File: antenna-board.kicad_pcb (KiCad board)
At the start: 2 copper layers, 42.4 x 42.4 mm, 2 parts, among them J1 Conn_01x01, U1 U.FLport

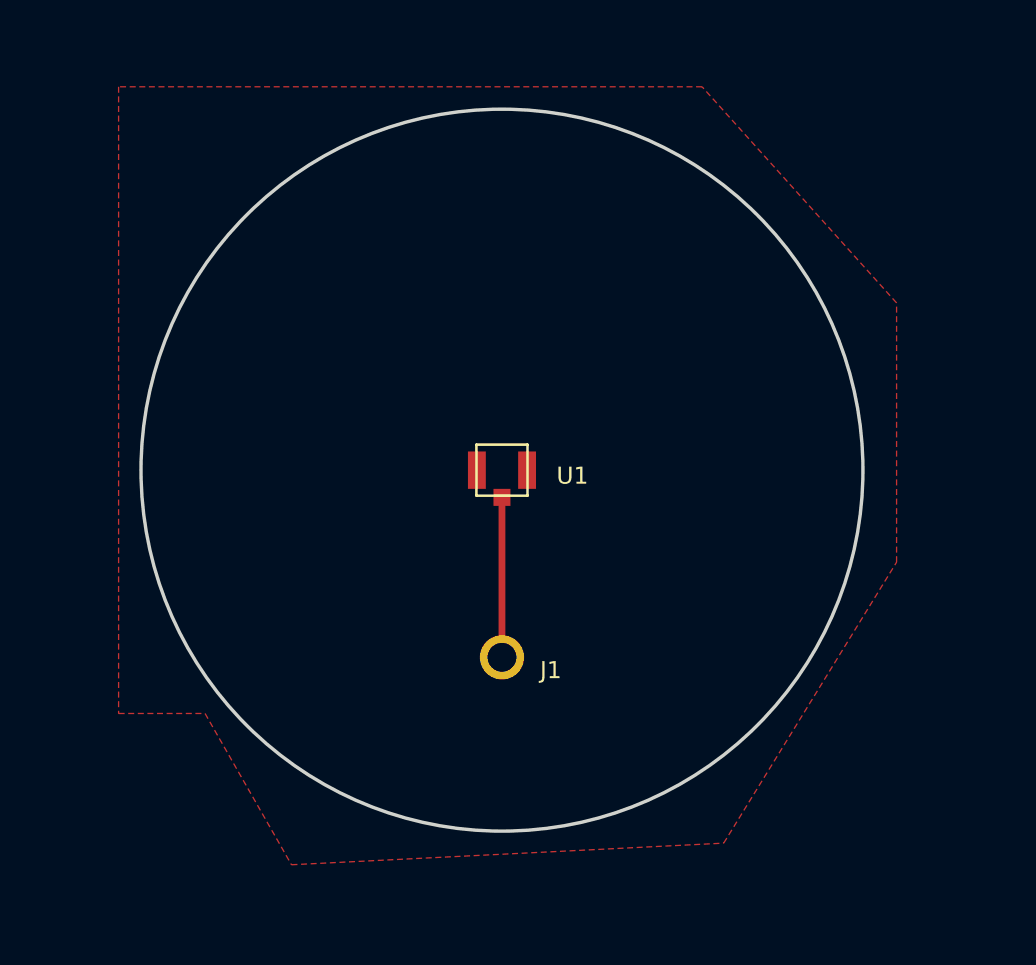
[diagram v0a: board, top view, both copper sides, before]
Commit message: Updated Trace Width and GNDs
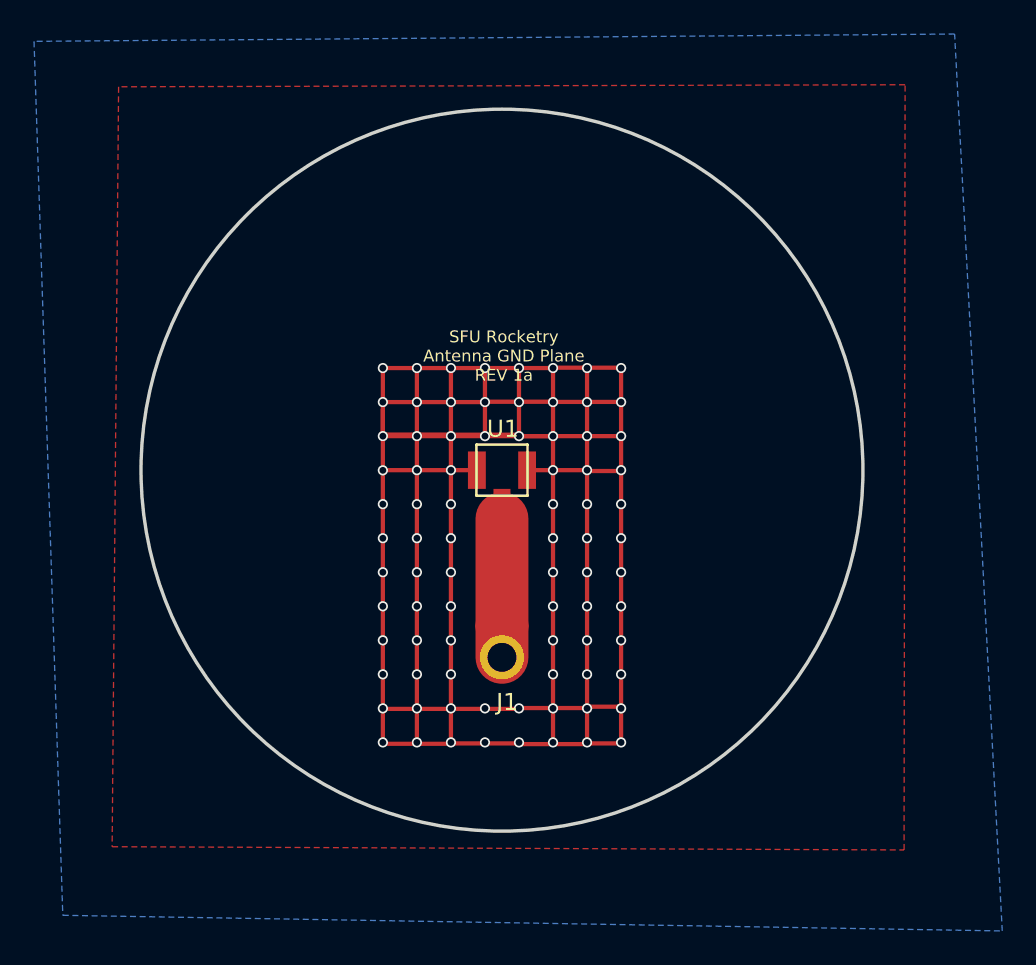
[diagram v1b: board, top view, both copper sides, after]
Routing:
- net GNDREF: track 0.00 -> 233.9 mm, vias 0 -> 82
- added copper zone on B.Cu, net GNDREF
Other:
- board text added: "SFU Rocketry Antenna GND Plane REV 1a"

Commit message: tried to make fill line but ran into conflicts. Also did Vias but wasn't sure about the two layers and how that worked...
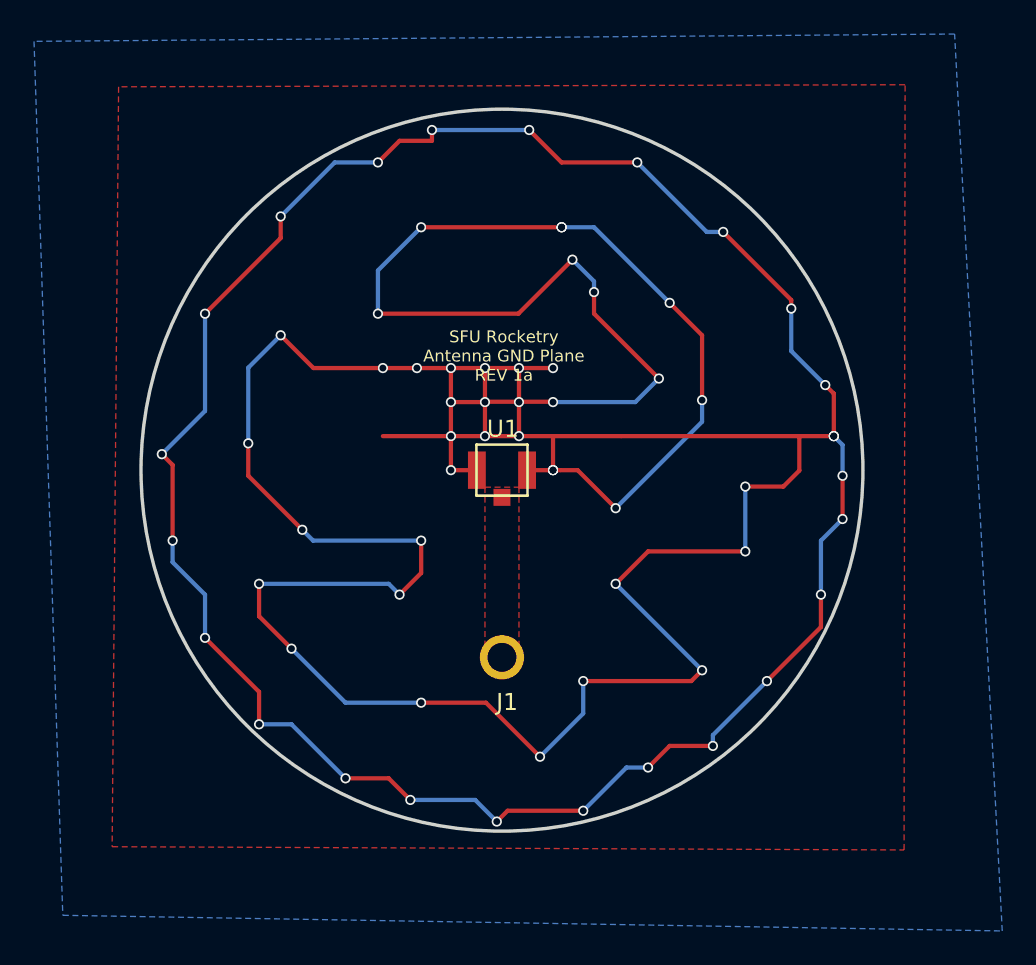
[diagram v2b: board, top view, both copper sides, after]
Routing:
- net GNDREF: track 233.9 -> 365.4 mm, vias 82 -> 65
- net DATA: track 9.87 -> 0.47 mm
- added copper zone on F.Cu, net DATA
